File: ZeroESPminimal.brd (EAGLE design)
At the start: 50.8 x 17.3 mm, 19 parts, among them IC2 MCP1703DB, X1 BU-SMA-G

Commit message: minor changes
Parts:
- moved C2 0.51 mm to (32.0, 33.0)
- moved C3 0.51 mm to (34.5, 33.0)
- moved C4 0.51 mm to (33.3, 37.3)
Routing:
- net SD_D1: track 8.64 -> 4.97 mm
- net VCC3: track 55.4 -> 54.1 mm
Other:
- outline, holes or cut-outs redrawn
- board text added: "hackaday.io /project/8252 /log/28949"
- board text added: "hackaday.io/davedarko"

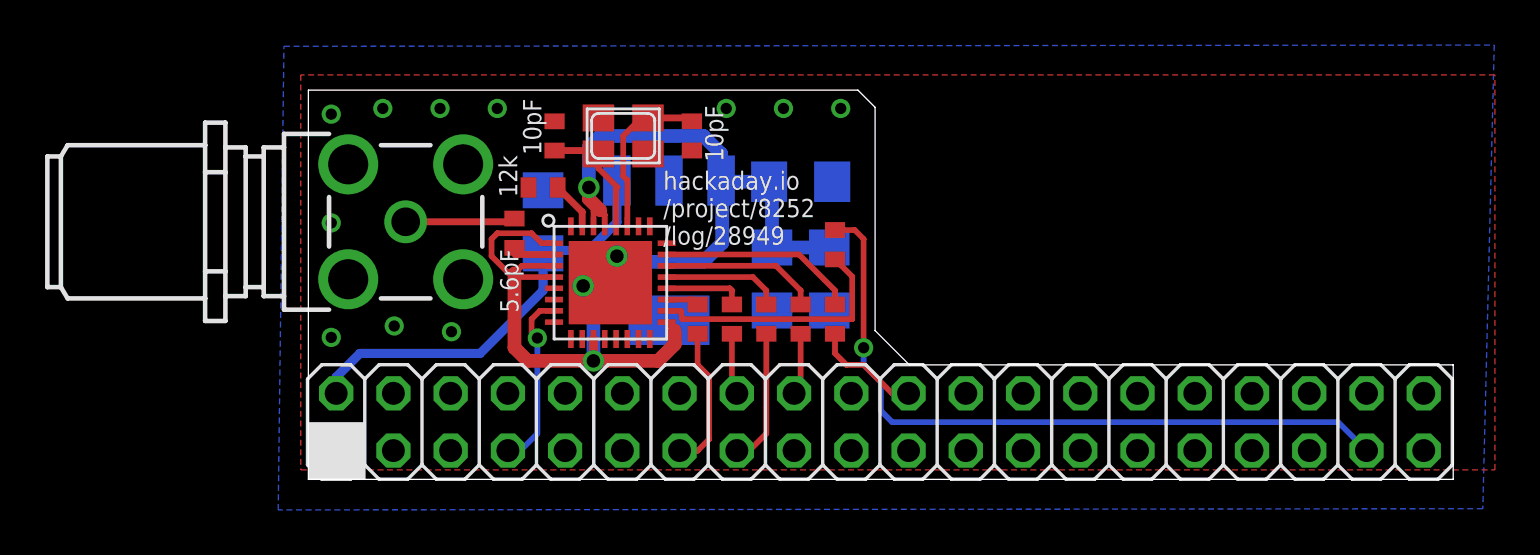
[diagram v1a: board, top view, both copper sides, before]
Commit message: connected ground pad of leo
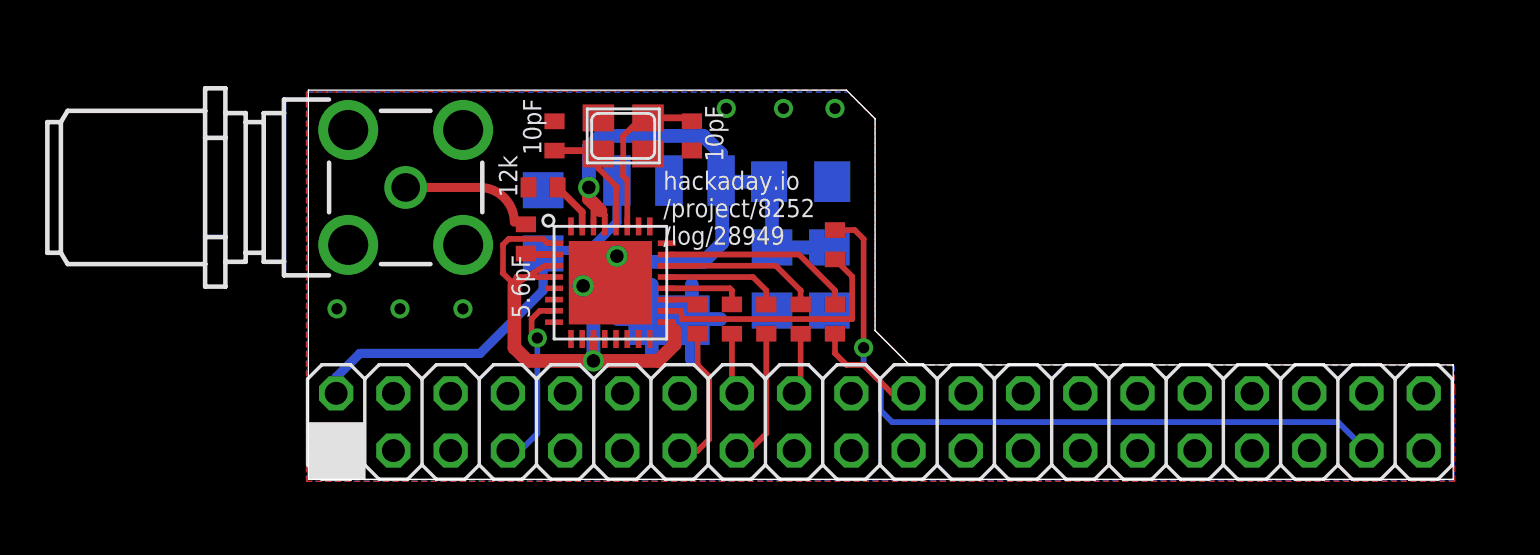
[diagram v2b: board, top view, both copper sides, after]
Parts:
- moved X1 1.52 mm to (15.7, 37.1)
- moved C5 0.57 mm to (21.1, 34.8)
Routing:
- net GND: track 0.00 -> 5.08 mm, vias 13 -> 8
- net N$3: track 4.89 -> 6.38 mm
- net VCC3: track 54.1 -> 53.2 mm
- net LNA: track 2.01 -> 1.27 mm
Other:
- outline, holes or cut-outs redrawn
